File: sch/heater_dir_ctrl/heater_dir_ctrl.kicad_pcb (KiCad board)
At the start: 2 copper layers, 93 parts, among them J10 heater, J11 heater, J12 10V, J13 10V, J14 10V, J3 UV, J4 SWD, J5 motor, J6 motor, J7 .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

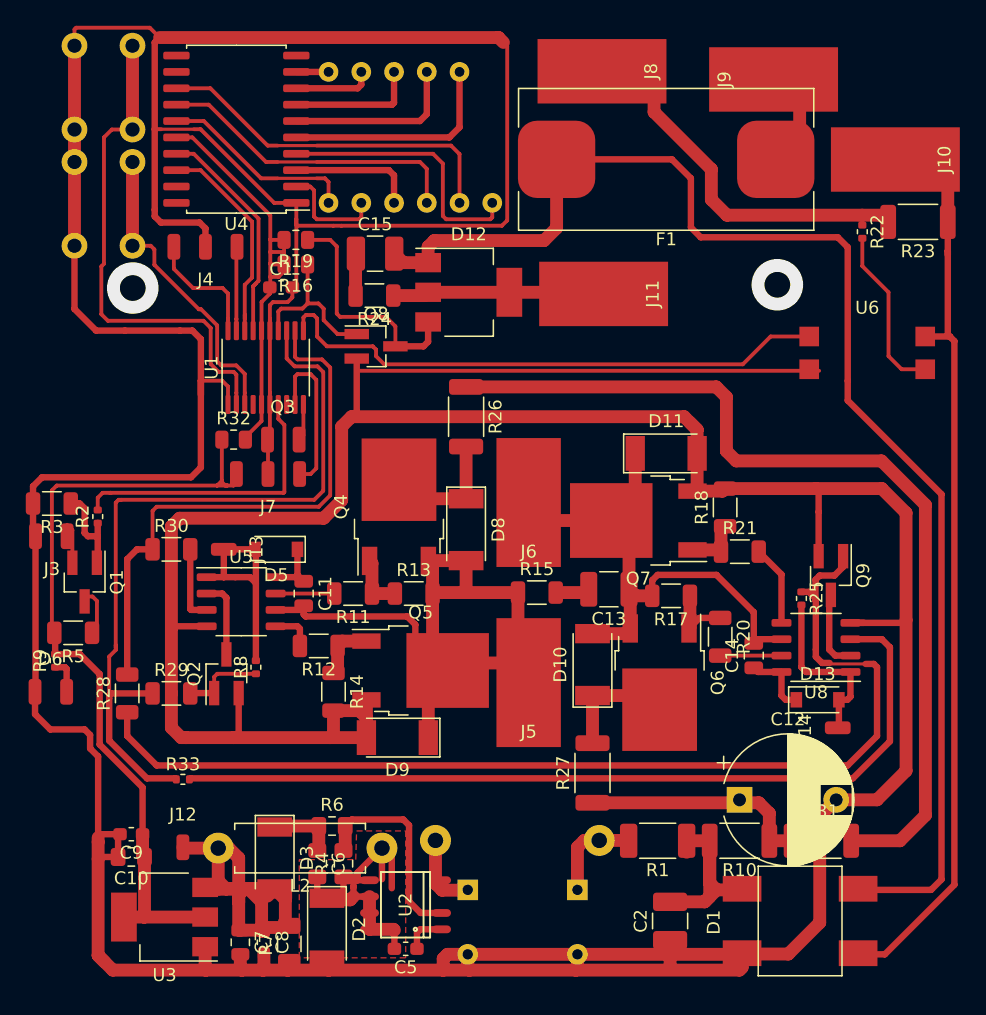
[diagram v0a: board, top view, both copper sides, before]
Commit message: 78l instead of 1117, synchronized pwm ok, not tested
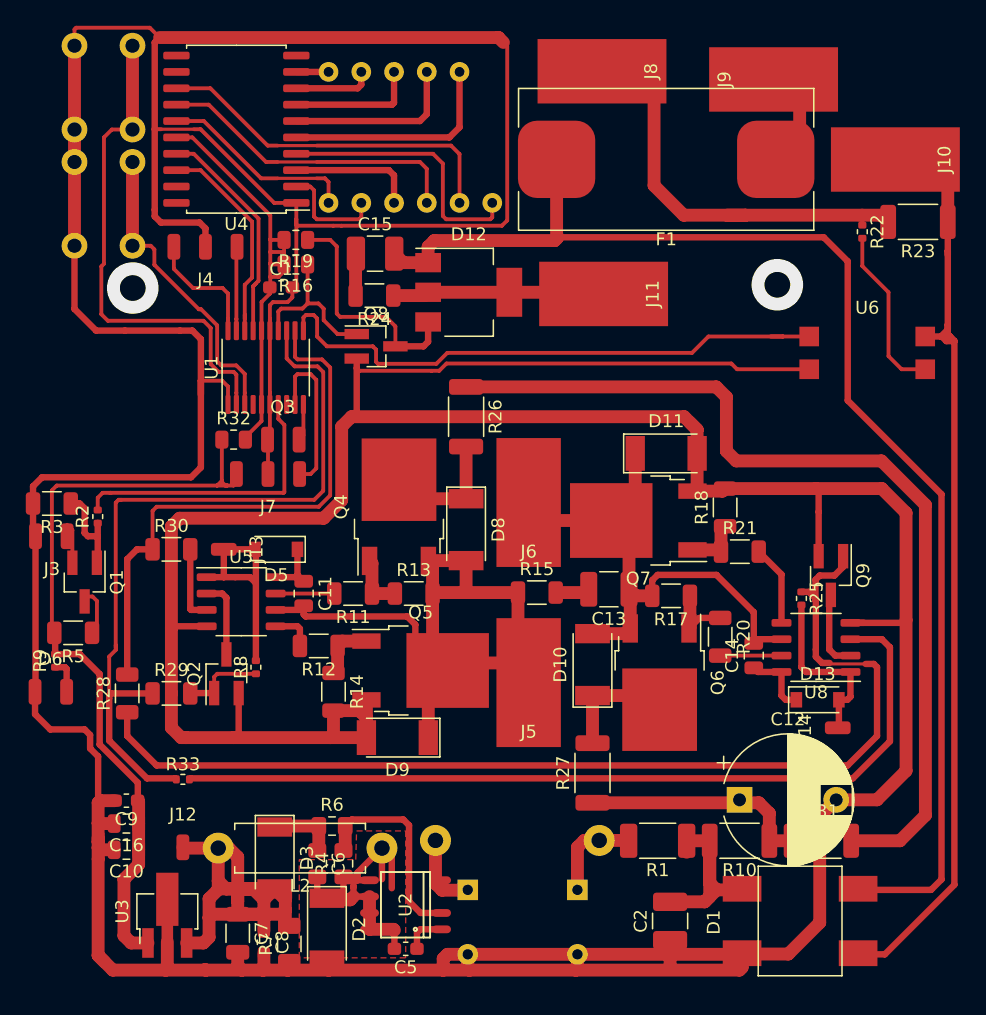
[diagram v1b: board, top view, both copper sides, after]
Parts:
- added C16: 10uF, Capacitor_SMD:C_0805_2012Metric, F.Cu at (30.1, 85.5)
- C10: footprint Capacitor_SMD:C_0805_2012Metric_Pad1.15x1.40mm_HandSolder -> Capacitor_SMD:C_0805_2012Metric
- C7: value 10uF -> 100uF; footprint Capacitor_SMD:C_0805_2012Metric -> Capacitor_SMD:C_1206_3216Metric
- U3: value AP1117-33 -> L78L33_SOT89; footprint Package_TO_SOT_SMD:SOT-223-3_TabPin2 -> Package_TO_SOT_SMD:SOT-89-3_Handsoldering
- moved C9 2.63 mm to (30.1, 83.8)
- moved C7 0.73 mm to (38.7, 94.0)
- moved C10 0.68 mm to (30.1, 87.6)
- moved U3 0.26 mm to (33.3, 92.6), turned to 90 degrees
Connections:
- U3 pad 1: GND -> +3.3VA
- U3 pad 2: +3.3VA -> GND
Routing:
- net +10V: track 71.2 -> 78.7 mm
- net NEUT: track 106.6 -> 102.0 mm
- net Net-(J8-Pad1): track 32.3 -> 35.7 mm
- net LINE: track 87.4 -> 90.4 mm
- net +3.3VA: track 62.9 -> 60.5 mm
- net Net-(U1-Pad11): track 43.9 -> 45.1 mm

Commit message: narkoman
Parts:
- R33: footprint Resistor_SMD:R_0402_1005Metric -> Resistor_SMD:R_1206_3216Metric
- U3: footprint Package_TO_SOT_SMD:SOT-89-3_Handsoldering -> Package_TO_SOT_SMD:SOT-89-3
- moved R33 49.3 mm to (83.8, 80.4)
- moved R25 7.58 mm to (85.1, 75.2), turned to 0 degrees
- moved J14 2.22 mm to (87.1, 76.8), turned to 0 degrees
- moved U3 1.31 mm to (34.1, 91.6)
- moved R8 1.27 mm to (40.2, 72.1)
- moved Q9 1.05 mm to (83.7, 66.3), turned to 90 degrees
- moved D13 0.97 mm to (83.8, 76.9)
- turned R28 to 270 degrees
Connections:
- Q9 pad 1: /LEFT -> Net-(Q9-Pad1)
- R25 pad 1: /LEFT -> Net-(Q9-Pad3)
- R28 pad 2: /LEFTO -> Net-(Q9-Pad1)
- R30 pad 1: /LEFTO -> /LEFT
- R8 pad 1: Net-(Q2-Pad1) -> Net-(Q2-Pad3)
- U1 pad 12: /LEFTO -> /LEFT
- U5 pad 2: Net-(Q2-Pad3) -> Net-(R30-Pad2)
- U5 pad 3: Net-(R30-Pad2) -> Net-(Q2-Pad3)
- U8 pad 2: Net-(Q9-Pad3) -> Net-(R33-Pad2)
- U8 pad 3: Net-(R33-Pad2) -> Net-(Q9-Pad3)
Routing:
- net Net-(Q9-Pad1): track 0.00 -> 71.3 mm
- net Net-(R33-Pad2): track 66.2 -> 14.7 mm
- net /RIGHT: track 60.2 -> 104.4 mm
- net /LEFTO: track 43.5 -> 0.00 mm
- net /LEFT: track 84.3 -> 42.8 mm
- net +10V: track 78.7 -> 68.1 mm
- net Net-(Q9-Pad3): track 6.13 -> 12.5 mm
- net Net-(Q2-Pad1): track 6.46 -> 1.86 mm
- net +3.3VA: track 60.5 -> 58.2 mm
- net Net-(R30-Pad2): track 6.24 -> 4.81 mm
- net Net-(C13-Pad1): track 42.2 -> 43.4 mm
- net Net-(Q2-Pad3): track 6.06 -> 7.26 mm
- net Net-(C14-Pad1): track 5.40 -> 6.46 mm
- net GND: track 530.0 -> 531.0 mm

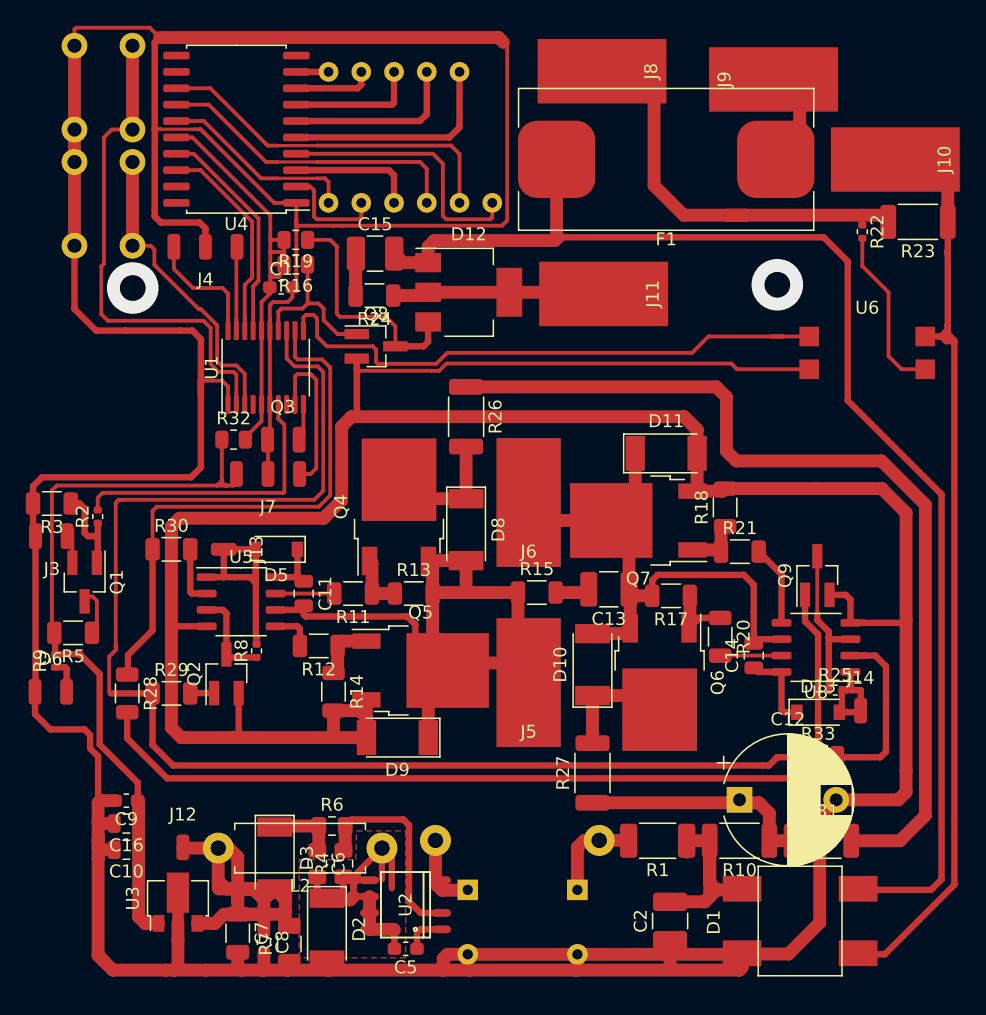
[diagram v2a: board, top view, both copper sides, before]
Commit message: new drivers
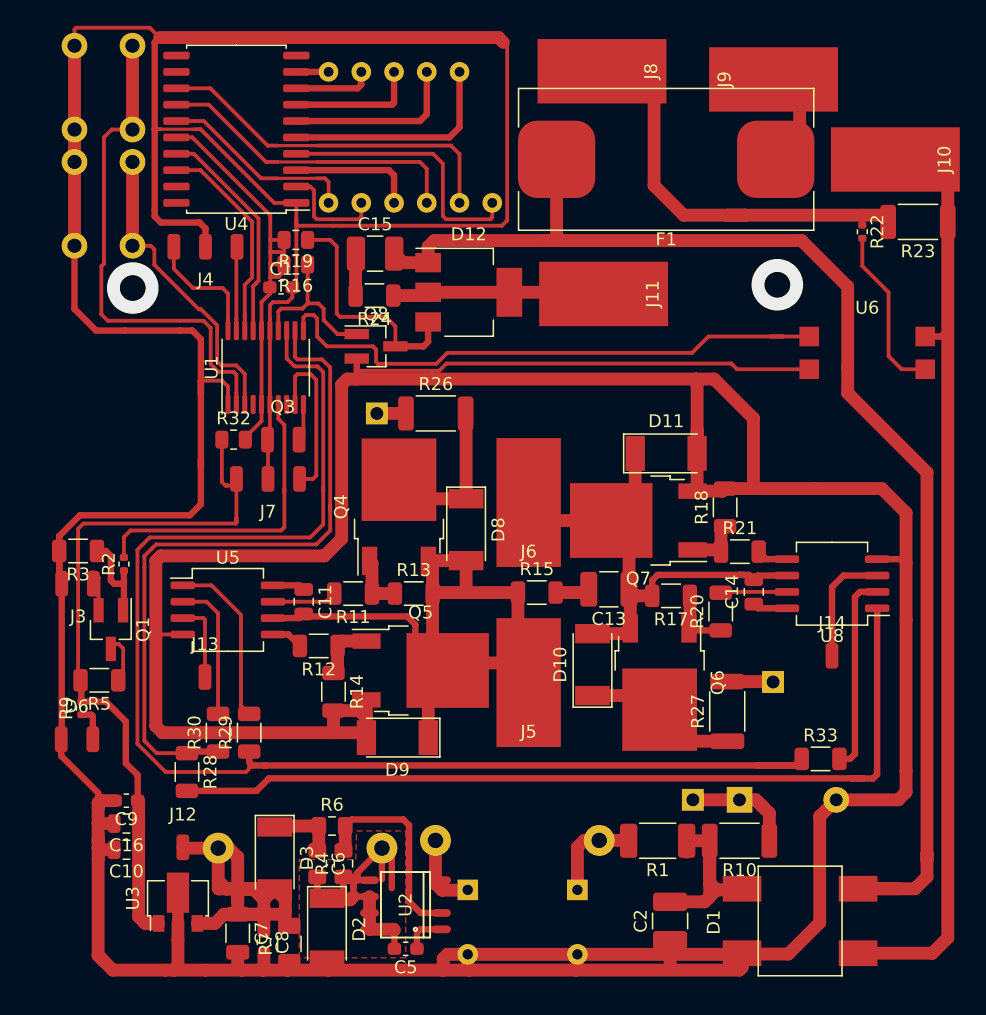
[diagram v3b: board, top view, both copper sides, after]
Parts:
- removed D13, D5: MBR0530, Diode_SMD:D_SOD-123
- removed Q2, Q9: DTD114E, Package_TO_SOT_SMD:SOT-23_Handsoldering
- removed R25, R8: 100k, Resistor_SMD:R_0402_1005Metric
- removed R31: 1, Resistor_SMD:R_2010_5025Metric
- added J1: 300V, Connector_PinHeader_2.54mm:PinHeader_1x01_P2.54mm_Vertical, B.Cu at (74.0, 83.7)
- added J15: 300V, Connector_PinHeader_2.54mm:PinHeader_1x01_P2.54mm_Vertical, B.Cu at (80.3, 74.5)
- added J2: 300V, Connector_PinHeader_2.54mm:PinHeader_1x01_P2.54mm_Vertical, B.Cu at (49.5, 53.7)
- C12, L2: moved to B.Cu
- U5, U8: value IRS2103 -> L6388; footprint Package_SO:SSOP-8_3.9x5.05mm_P1.27mm -> Package_SO:SO-8_5.3x6.2mm_P1.27mm
- moved R30 14.7 mm to (37.2, 78.5), turned to 90 degrees
- moved R27 11.5 mm to (76.7, 76.8)
- moved J13 10.0 mm to (36.2, 74.2), turned to 0 degrees
- moved R28 7.66 mm to (34.8, 81.5)
- moved R29 6.76 mm to (39.6, 78.5), turned to 90 degrees
- moved U8 5.09 mm to (84.8, 66.9)
- moved C14 4.94 mm to (78.8, 67.6)
- moved J14 4.80 mm to (84.8, 72.5)
- moved R9 4.21 mm to (26.6, 76.6)
- moved J3 4.21 mm to (26.4, 66.9)
- moved R2 4.21 mm to (29.9, 65.4)
- moved D6 4.21 mm to (26.2, 79.0)
- moved Q1 4.21 mm to (28.9, 70.5)
- moved R3 4.21 mm to (26.4, 64.4)
- moved R5 4.21 mm to (28.0, 74.4)
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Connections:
- R27 pad 1: Net-(C12-Pad1) -> Net-(D10-Pad1)
- R27 pad 2: Net-(D10-Pad1) -> Net-(J15-Pad1)
- R28 pad 2: Net-(Q9-Pad1) -> Net-(R28-Pad2)
- R29 pad 2: Net-(Q2-Pad1) -> Net-(R29-Pad2)
- U5 pad 1: +10V -> Net-(R29-Pad2)
- U5 pad 3: Net-(Q2-Pad3) -> +10V
- U8 pad 1: +10V -> Net-(R28-Pad2)
- U8 pad 3: Net-(Q9-Pad3) -> +10V
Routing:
- net Net-(Q9-Pad1): track 71.3 -> 0.00 mm
- net Net-(J2-Pad1): track 72.5 -> 2.69 mm
- net Net-(R28-Pad2): track 0.00 -> 67.8 mm
- net /LEFT: track 42.8 -> 56.3 mm
- net Net-(R29-Pad2): track 0.00 -> 13.4 mm
- net Net-(Q9-Pad3): track 12.5 -> 0.00 mm
- net +10V: track 68.1 -> 59.1 mm
- net Net-(C12-Pad1): track 17.9 -> 9.02 mm
- net Net-(Q2-Pad3): track 7.26 -> 0.00 mm
- net Net-(R30-Pad2): track 4.81 -> 10.9 mm
- net LINE: track 90.4 -> 95.6 mm
- net GND: track 531.0 -> 535.8 mm
- net Net-(C13-Pad1): track 43.4 -> 39.5 mm
- net Net-(R21-Pad2): track 6.26 -> 2.43 mm
- net Net-(C14-Pad1): track 6.46 -> 2.70 mm
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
